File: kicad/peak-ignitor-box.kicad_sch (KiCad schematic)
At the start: 145 parts, among them J1 +24V, J10 SW, J11 Conn_01x01, J12 Conn_01x01, J13 Conn_01x01, J14 Conn_01x01, J15 GND, J2 GND, J3 PROG, J4 JTAG, J5 BATT, J6 GND, J7 +12V, J8 Barrel_Jack, J9 BATT-sw, Q1 BSS138, Q2 BSS138, Q3 IRLML9301, Q4 NVTFS5C454NLWFTAG, Q5 NVTFS5C454NLWFTAG, Q6 NVTFS5C454NLWFTAG, Q7 NVTFS5C454NLWFTAG, Q8 NVTFS5C454NLWFTAG, Q9 NVTFS5C454NLWFTAG, SW1 GT-TC029B-H025-L1N, SW2 GT-TC029B-H025-L1N, SW4 SW_Push, U1 TMP1075, U2 TMP1075, U3 ESP32-S3-MINI-1, U4 BQ24600, U5 AP3211, U6 LM51770DCPR, X1 20A-spare, X2 20A-spare, X3 20A-spare

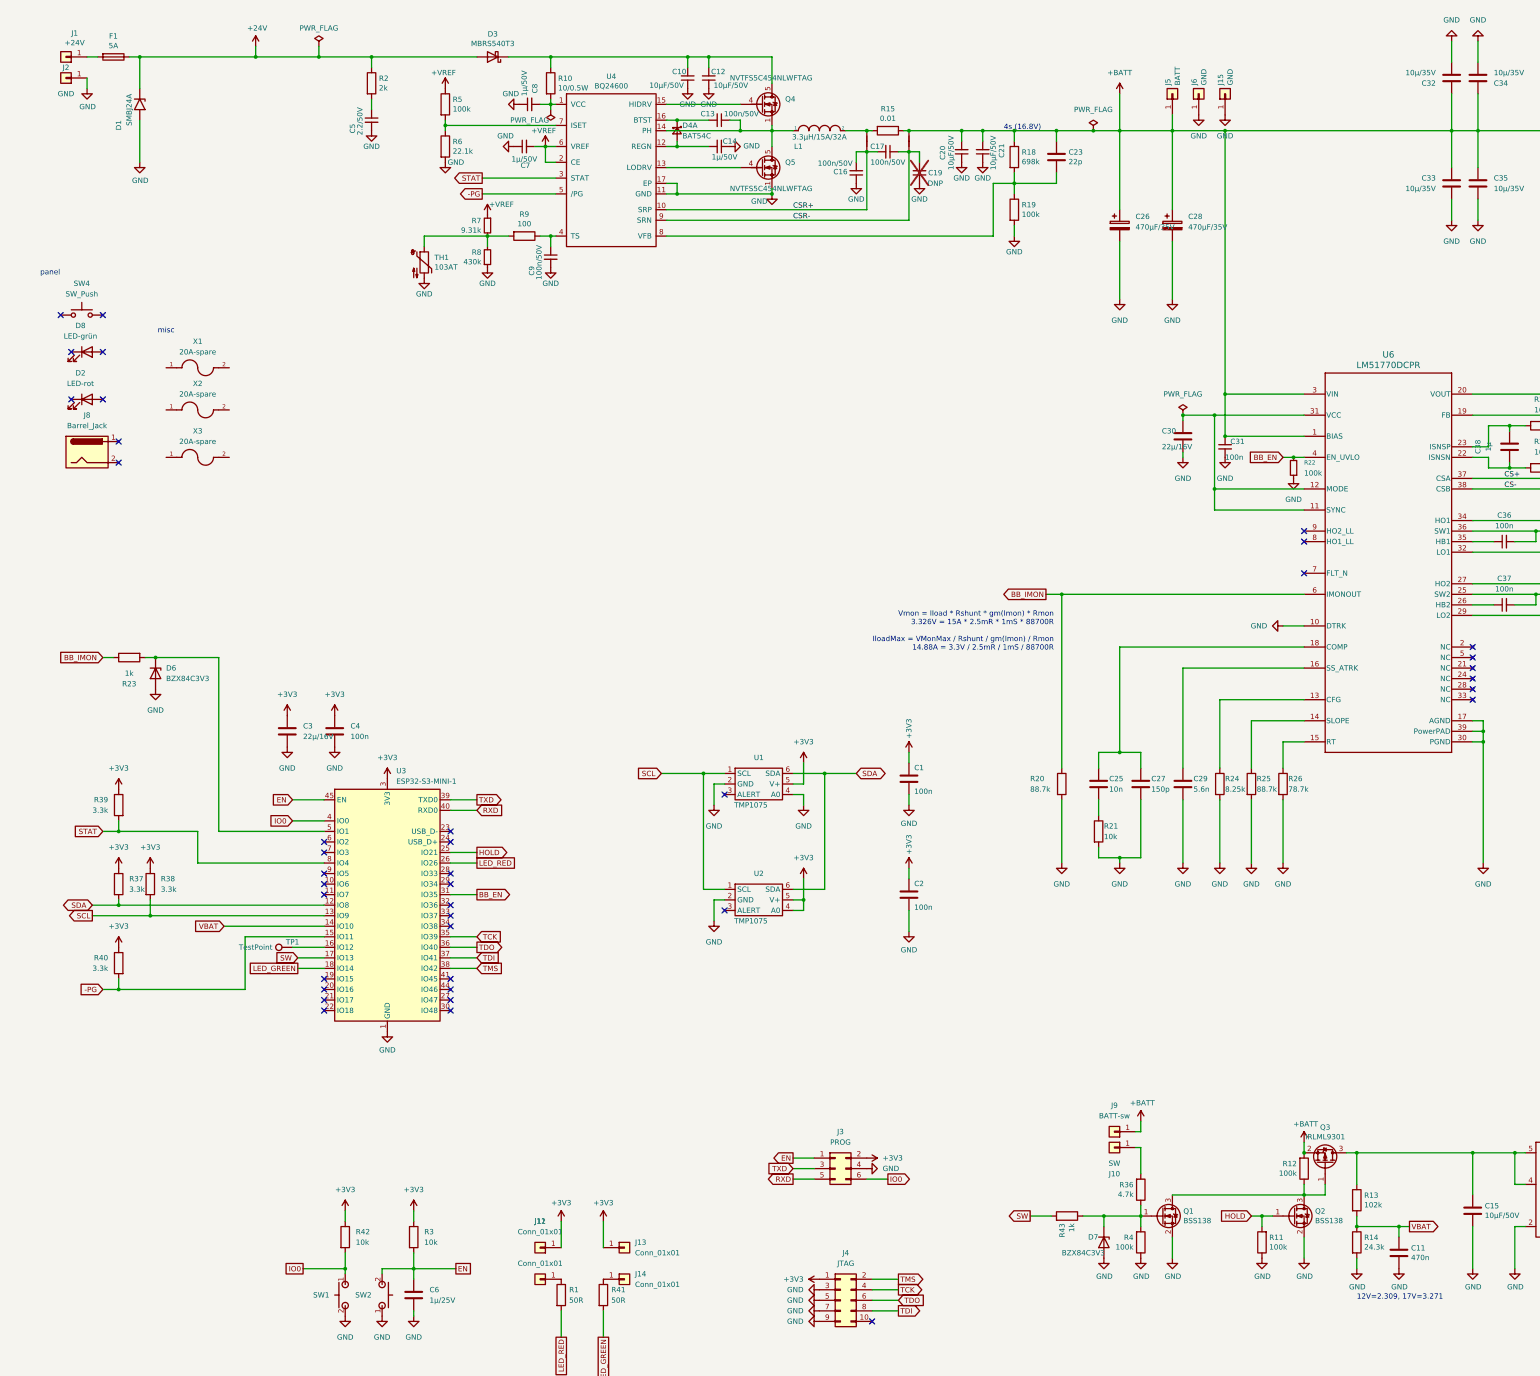
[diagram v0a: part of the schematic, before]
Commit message: updated gerbers, bom, some bug fixes on schematic and board
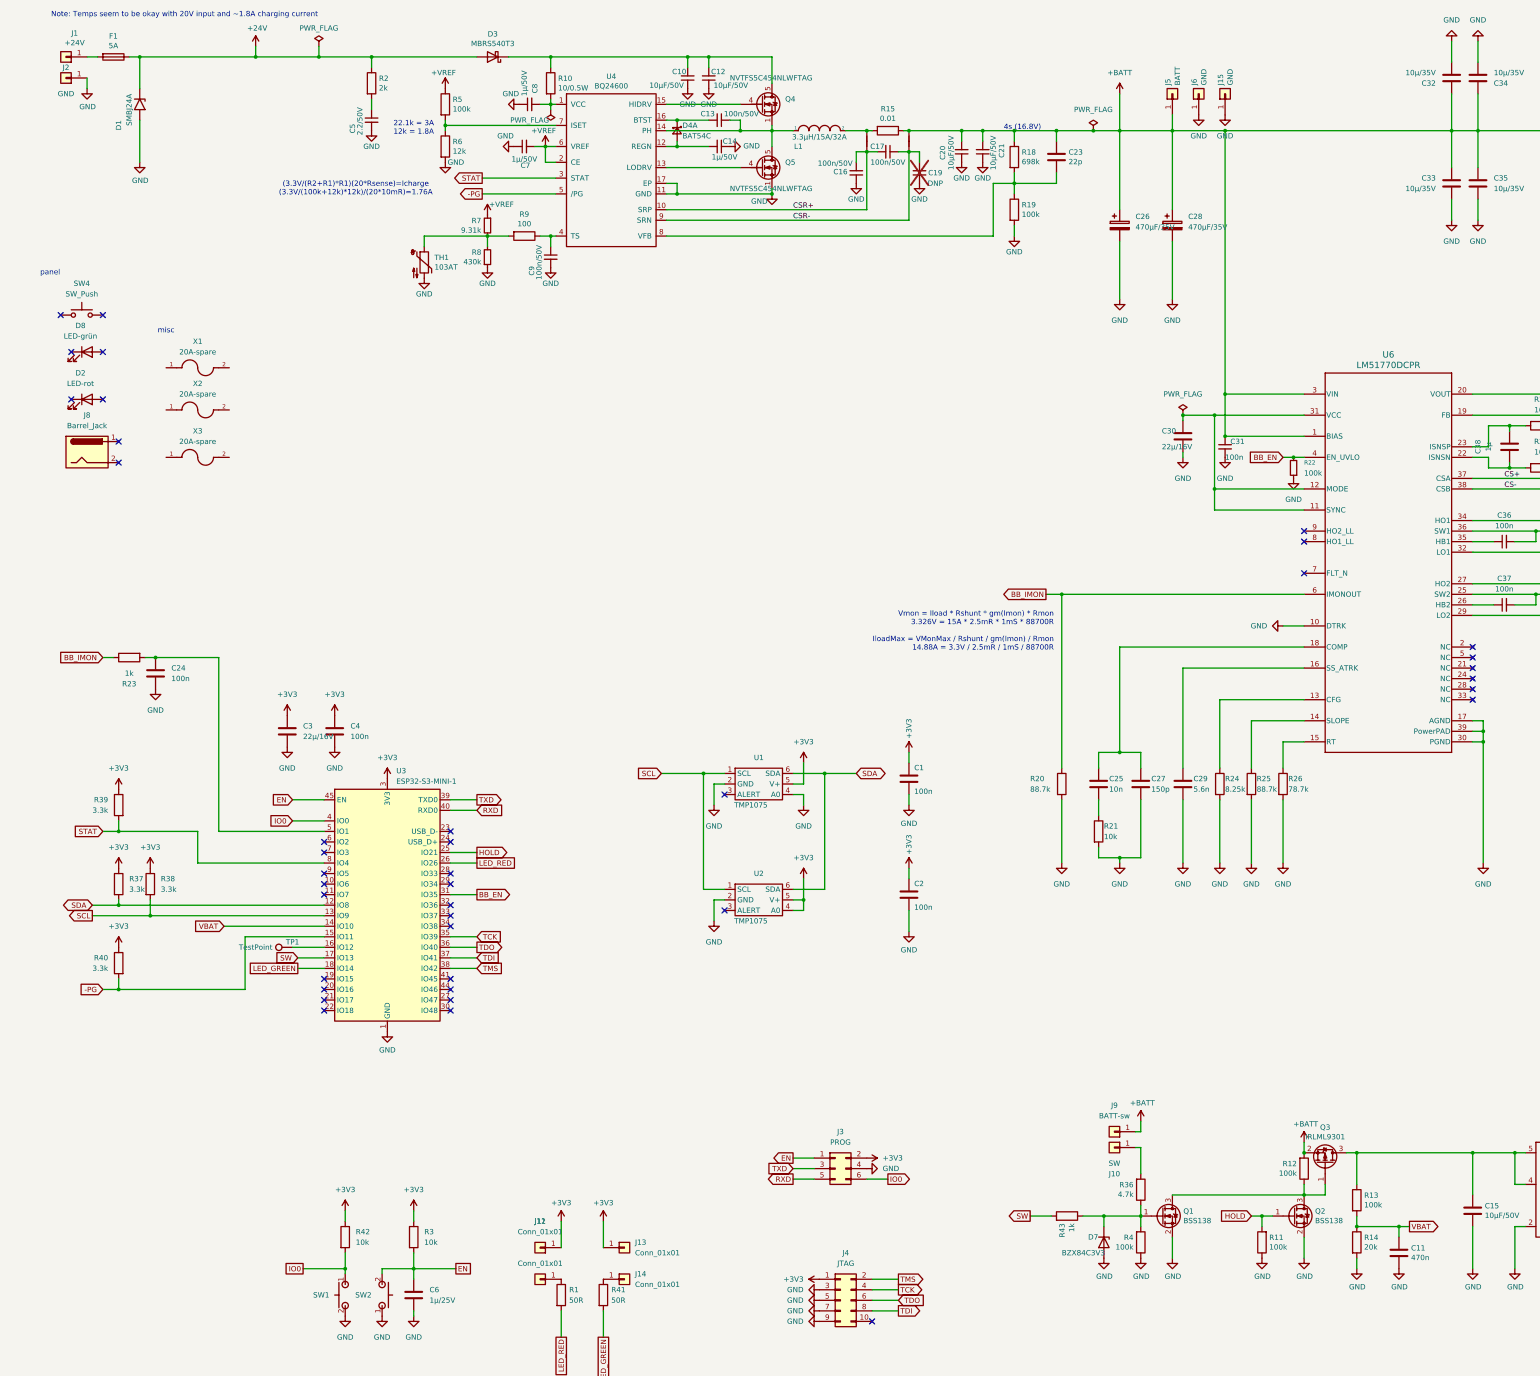
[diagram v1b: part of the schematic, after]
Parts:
- removed D6: BZX84C3V3, Package_TO_SOT_SMD:SOT-23, symbol Diode:BZX84Cxx
- added C24: 100n, Capacitor_SMD:C_0805_2012Metric, symbol Device:C
- D7: Distributor D -> (none); Manufacturer BZX84C15-TP -> (none); OrderNr BZX84C15-TPMSCT-ND -> (none)
- R13: value 102k -> 100k
- R14: value 24.3k -> 20k
- R6: value 22.1k -> 12k
- SW4: Manufacturer RP3502MBRED -> RP3502MARED; OrderNr EG1939-ND -> EG1938-ND
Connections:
- net GND: now also C24.2
- net at R23.2, U3.5 (IO1): now also C24.1
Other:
- note added: "(3.3V/(R2+R1)*R1)(20*Rsense)=Icharge (3.3V/(100k+12k)*12k)/(20*10mR)=1.76A"
- note added: "22.1k = 3A 12k = 1.8A"
- note added: "Note: Temps seem to be okay with 20V input and ~1.8A charging current"
- note removed: "12V=2.309, 17V=3.271"
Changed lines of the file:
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@@
 	(generator_version "9.0")
 	(paper "A2")
+	(text "Note: Temps seem to be okay with 20V input and ~1.8A charging current"
+		(exclude_from_sim no)
+		(at 53.975 78.74 0)
+		(effects
+			(font
+				(size 1.27 1.27)
+			)
+		)
+	)
+	(text "(3.3V/(R2+R1)*R1)(20*Rsense)=Icharge\n(3.3V/(100k+12k)*12k)/(20*10mR)=1.76A"
+		(exclude_from_sim no)
+		(at 95.25 120.65 0)
+		(effects
+			(font
+				(size 1.27 1.27)
+			)
+		)
+	)
 	(text "Vmon = Iload * Rshunt * gm(Imon) * Rmon\n3.326V = 15A * 2.5mR * 1mS * 88700R\n\nIloadMax = VMonMax / Rshunt / gm(Imon) / Rmon\n14.88A = 3.3V / 2.5mR / 1mS / 88700R"
 		(exclude_from_sim no)
@@
 		)
 	)
-	(text "12V=2.309, 17V=3.271"
+	(text "misc"
 		(exclude_from_sim no)
-		(at 336.55 388.62 0)
+		(at 49.53 154.94 0)
 		(effects
 			(font
 				(size 1.27 1.27)
 			)
-			(justify left bottom)
 		)
 	)
-	(text "misc"
+	(text "22.1k = 3A\n12k = 1.8A"
 		(exclude_from_sim no)
-		(at 49.53 154.94 0)
+		(at 109.22 106.045 0)
 		(effects
 			(font
@@
 	)
 	(junction
+		(at 46.99 233.68)
+		(diameter 0)
+		(color 0 0 0 0)
+	)
+	(junction
 		(at 430.53 160.02)
 		(diameter 0)
@@
 	)
 	(junction
-		(at 46.99 233.68)
-		(diameter 0)
-		(color 0 0 0 0)
-	)
-	(junction
 		(at 407.67 370.84)
 		(diameter 0)
@@
 	(wire
 		(pts
+			(xy 46.99 233.68) (xy 62.23 233.68)
+		)
+		(stroke
+			(width 0)
+			(type default)
+		)
+	)
+	(wire
+		(pts
 			(xy 116.84 105.41) (xy 143.51 105.41)
 		)
@@
 	(wire
 		(pts
-			(xy 46.99 233.68) (xy 62.23 233.68)
-		)
-		(stroke
-			(width 0)
-			(type default)
-		)
-	)
-	(wire
-		(pts
 			(xy 38.1 275.59) (xy 57.15 275.59)
 		)
@@
 			)
 		)
-		(property "Value" "22.1k"
+		(property "Value" "12k"
 			(at 118.618 111.633 0)
 			(effects
@@
 			)
 		)
-		(property "Value" "102k"
+		(property "Value" "100k"
 			(at 338.328 365.633 0)
 			(effects
@@
 			)
 		)
-		(property "Value" "24.3k"
+		(property "Value" "20k"
 			(at 338.328 375.793 0)
 			(effects
@@
 	)
 	(symbol
-		(lib_id "Diode:BZX84Cxx")
-		(at 46.99 237.49 270)
-		(unit 1)
-		(exclude_from_sim no)
-		(in_bom yes)
-		(on_board yes)
-		(dnp no)
-		(fields_autoplaced yes)
-		(property "Reference" "D6"
-			(at 49.53 236.2199 90)
-			(effects
-				(font
-					(size 1.27 1.27)
-				)
-				(justify left)
-			)
-		)
-		(property "Value" "BZX84C3V3"
-			(at 49.53 238.7599 90)
-			(effects
-				(font
-					(size 1.27 1.27)
-				)
-				(justify left)
-			)
-		)
-		(property "Footprint" "Package_TO_SOT_SMD:SOT-23"
-			(at 46.99 237.49 0)
-			(effects
-				(font
-					(size 1.27 1.27)
-				)
-				(hide yes)
-			)
-		)
-		(property "Datasheet" "https://diotec.com/tl_files/diotec/files/pdf/datasheets/bzx84c2v4.pdf"
-			(at 46.99 237.49 0)
-			(effects
-				(font
-					(size 1.27 1.27)
-				)
-				(hide yes)
-			)
-		)
-		(property "Description" "300mW Zener Diode, SOT-23"
-			(at 46.99 237.49 0)
-			(effects
-				(font
-					(size 1.27 1.27)
-				)
-				(hide yes)
-			)
-		)
-		(pin "1"
-		)
-		(pin "3"
-		)
-		(pin "2"
-		)
-		(instances
-			(project ""
-				(path "/f83baf2c-645b-4eaa-9e2e-814c12002028"
-					(reference "D6")
-					(unit 1)
-				)
-			)
-		)
-	)
-	(symbol
 		(lib_id "Connector_Generic:Conn_01x01")
 		(at 160.02 375.92 0)
@@
 			)
 		)
-		(property "Manufacturer" "RP3502MBRED"
+		(property "Manufacturer" "RP3502MARED"
 			(at 29.21 151.13 0)
 			(effects
@@
 			)
 		)
-		(property "OrderNr" "EG1939-ND"
+		(property "OrderNr" "EG1938-ND"
 			(at 29.21 151.13 0)
 			(effects
@@
 			)
 		)
-		(property "Datasheet" "https://diotec.com/tl_files/diotec/files/pdf/datasheets/bzx84c2v4.pdf"
+		(property "Datasheet" ""
 			(at 275.59 374.65 0)
 			(effects
@@
 			)
 		)
-		(property "Description" "300mW Zener Diode, SOT-23"
+		(property "Description" ""
 			(at 275.59 374.65 0)
 			(effects
@@
 			)
 		)
-		(property "Distributor" "D"
-			(at 275.59 374.65 90)
-			(effects
-				(font
-					(size 1.27 1.27)
-				)
-				(hide yes)
-			)
-		)
-		(property "Manufacturer" "BZX84C15-TP"
-			(at 275.59 374.65 90)
-			(effects
-				(font
-					(size 1.27 1.27)
-				)
-				(hide yes)
-			)
-		)
-		(property "OrderNr" "BZX84C15-TPMSCT-ND"
-			(at 275.59 374.65 90)
-			(effects
-				(font
-					(size 1.27 1.27)
-				)
-				(hide yes)
-			)
-		)
 		(pin "1"
 		)
@@
 					(unit 1)
 				)
+			)
+		)
+	)
+	(symbol
+		(lib_id "Device:C")
+		(at 46.99 237.49 0)
+		(unit 1)
+		(exclude_from_sim no)
+		(in_bom yes)
+		(on_board yes)
+		(dnp no)
+		(fields_autoplaced yes)
+		(property "Reference" "C24"
+			(at 50.8 236.2199 0)
+			(effects
+				(font
+					(size 1.27 1.27)
+				)
+				(justify left)
+			)
+		)
+		(property "Value" "100n"
+			(at 50.8 238.7599 0)
+			(effects
+				(font
+					(size 1.27 1.27)
+				)
+				(justify left)
+			)
+		)
+		(property "Footprint" "Capacitor_SMD:C_0805_2012Metric"
+			(at 47.9552 241.3 0)
+			(effects
+				(font
+					(size 1.27 1.27)
+				)
+				(hide yes)
+			)
+		)
+		(property "Datasheet" ""
+			(at 46.99 237.49 0)
+			(effects
+				(font
+					(size 1.27 1.27)
+				)
+				(hide yes)
+			)
+		)
+		(property "Description" "Unpolarized capacitor"
+			(at 46.99 237.49 0)
+			(effects
+				(font
+					(size 1.27 1.27)
+				)
+				(hide yes)
+			)
+		)
+		(pin "1"
+		)
+		(pin "2"
+		)
+		(instances
+			(project "peak-ignitor-box"
+				(path "/f83baf2c-645b-4eaa-9e2e-814c12002028"
+					(reference "C24")
+					(unit 1)
+				)
